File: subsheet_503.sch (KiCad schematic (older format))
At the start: 39 parts, among them Q500 LM78L82_TO92, U504 LF347N_mu, U505 MF4CN-100_PHY, U506 MF4CN-100_PHY, U507 LF347N_mu

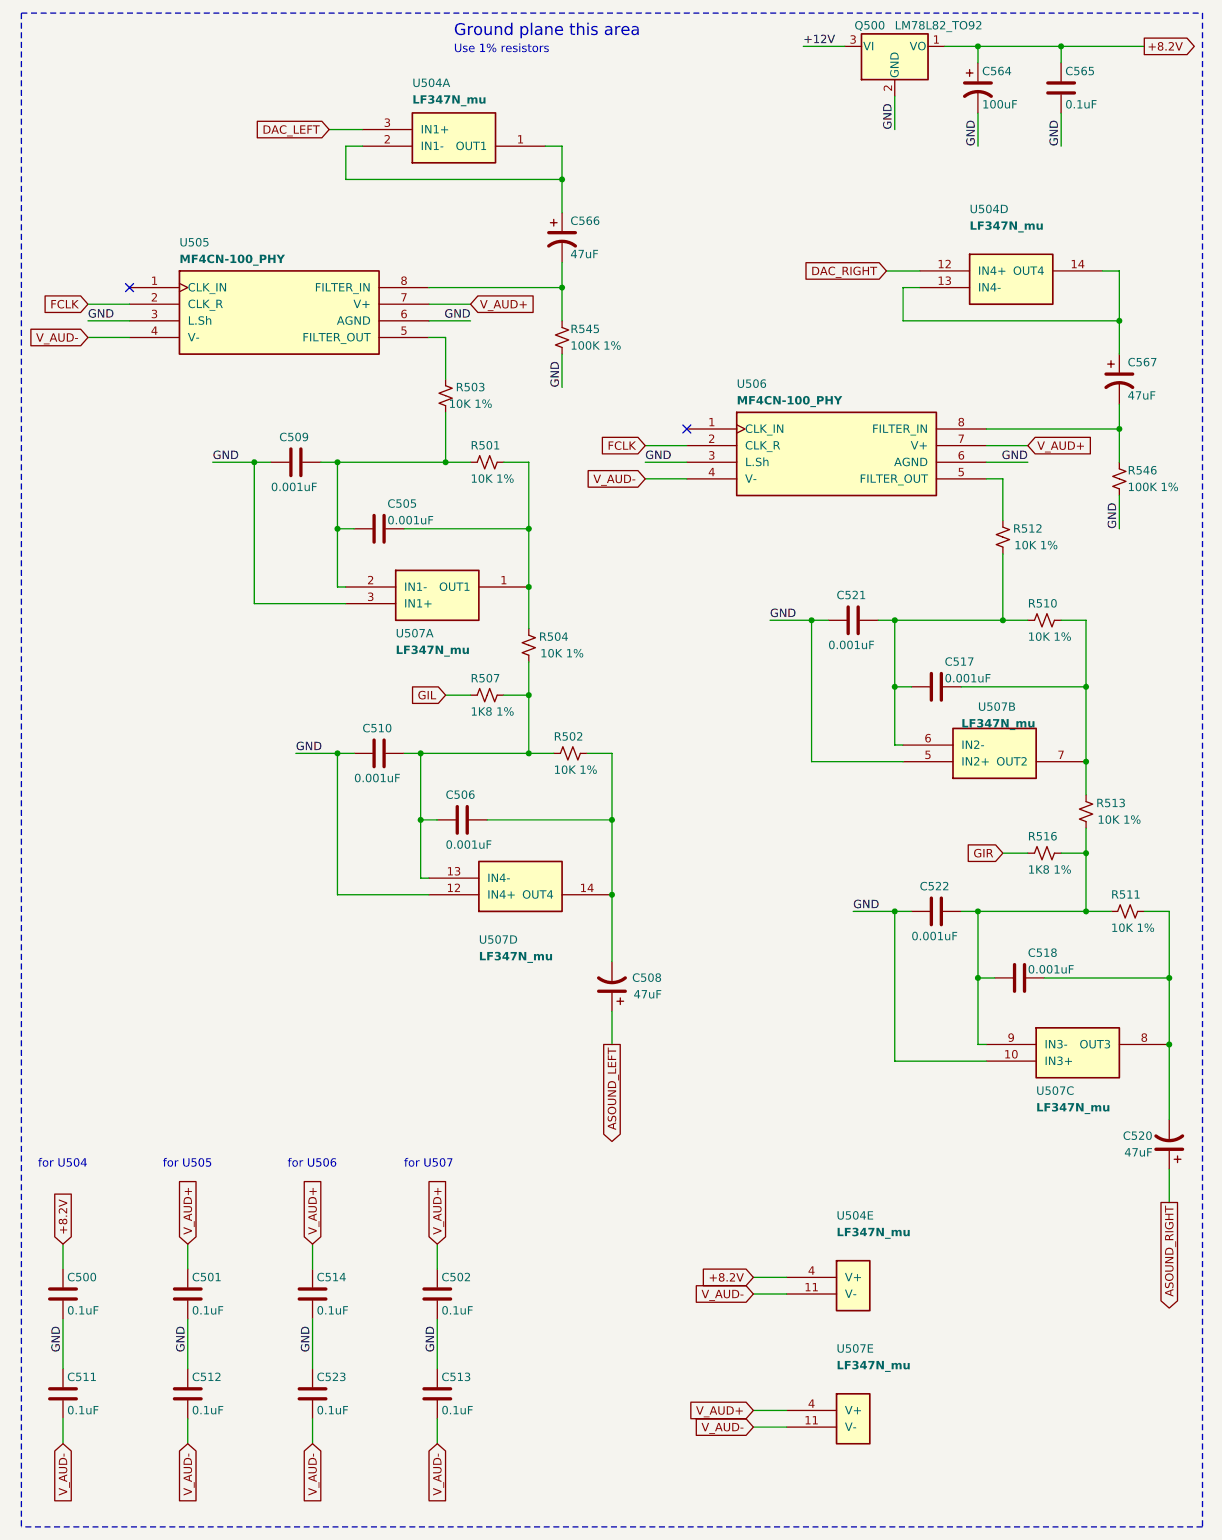
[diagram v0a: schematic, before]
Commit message: Resolves #12 : Use the reference 'CP?' for polarized capacitors
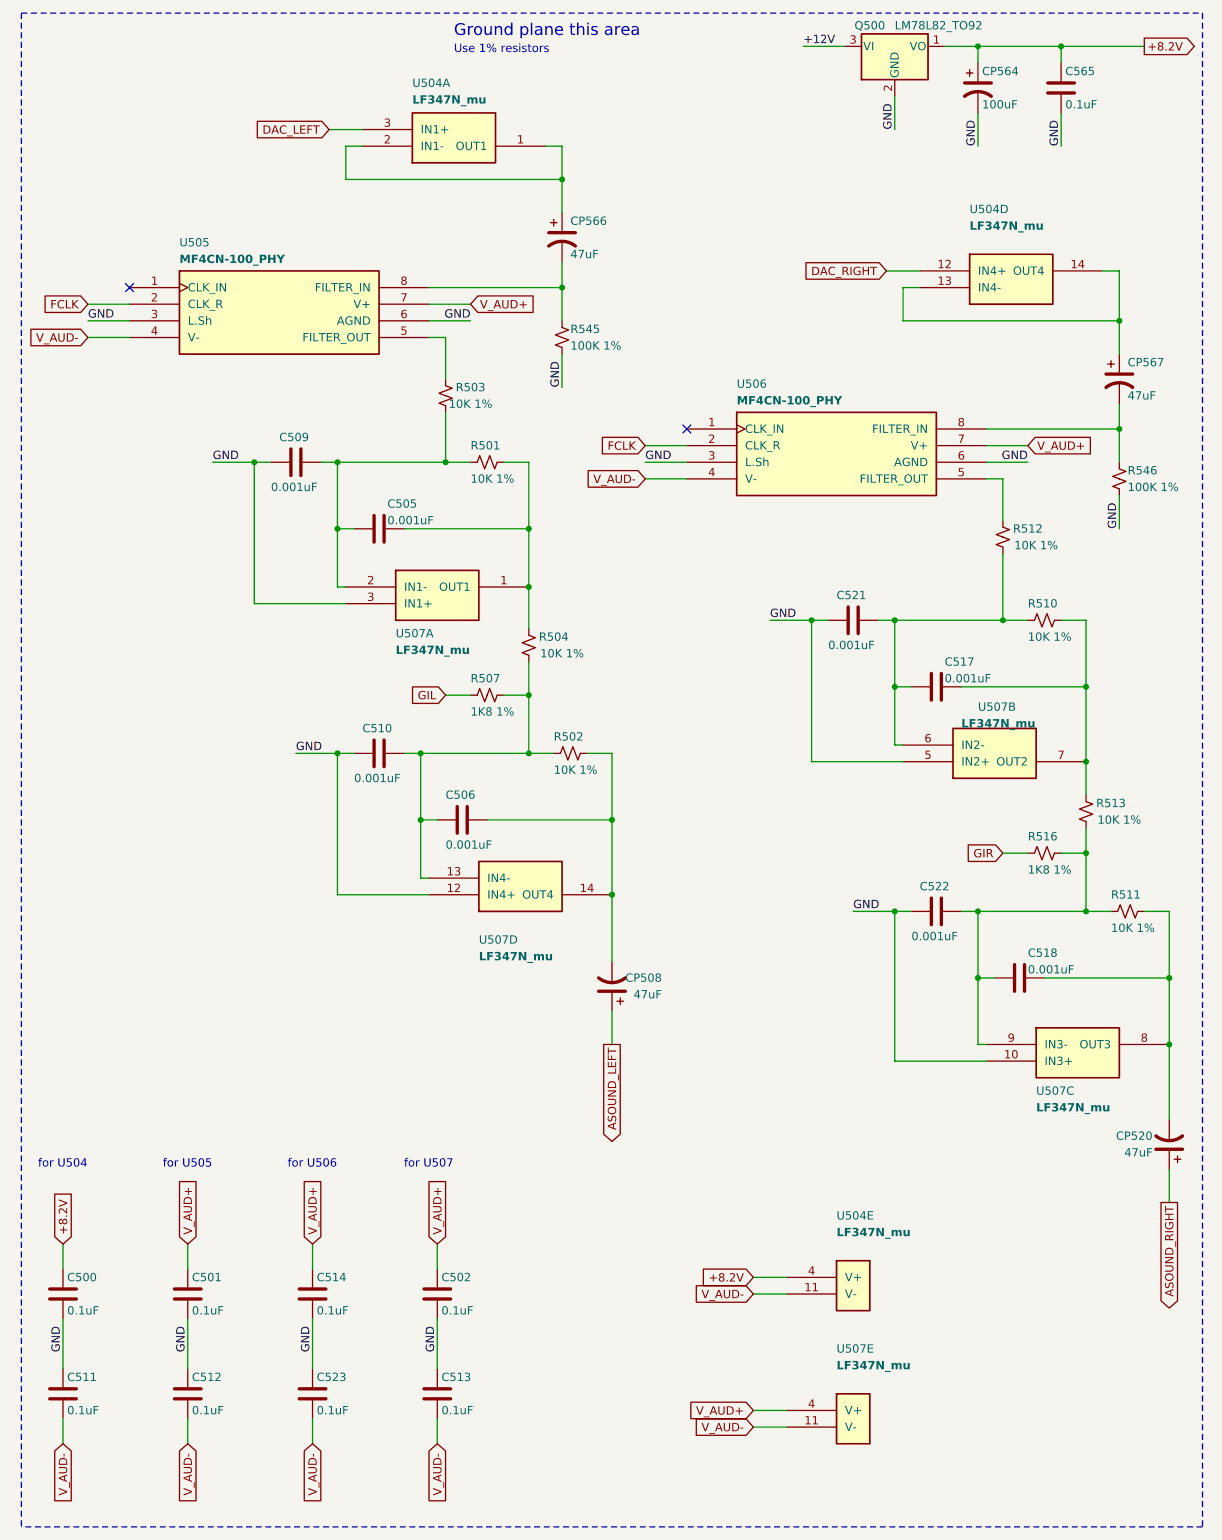
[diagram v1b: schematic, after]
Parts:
- renumbered C508 to CP508, C520 to CP520, C564 to CP564, C566 to CP566, C567 to CP567
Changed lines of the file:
@@
 AR Path="/60B8B7AD/60D196C8" Ref="C?"  Part="1"
 AR Path="/60C95DE8/60D196C8" Ref="C?"  Part="1"
-AR Path="/60CC3B10/60D196C8" Ref="C566"  Part="1"
-F 0 "C566" H 3900 2050 50  0000 L CNN
+AR Path="/60CC3B10/60D196C8" Ref="CP566"  Part="1"
+F 0 "CP566" H 3900 2050 50  0000 L CNN
 F 1 "47uF" H 3900 1850 50  0000 L CNN
 F 2 "commons_passives_THT:Passive_THT_capacitor_polarized_rad_D5.08mm_P2.54mm_H12.70mm" H 3850 1950 50  0001 C CNN
@@
 AR Path="/60B8B7AD/60DEF28D" Ref="C?"  Part="1"
 AR Path="/60C95DE8/60DEF28D" Ref="C?"  Part="1"
-AR Path="/60CC3B10/60DEF28D" Ref="C567"  Part="1"
-F 0 "C567" H 7250 2900 50  0000 L CNN
+AR Path="/60CC3B10/60DEF28D" Ref="CP567"  Part="1"
+F 0 "CP567" H 7250 2900 50  0000 L CNN
 F 1 "47uF" H 7250 2700 50  0000 L CNN
 F 2 "commons_passives_THT:Passive_THT_capacitor_polarized_rad_D5.08mm_P2.54mm_H12.70mm" H 7200 2800 50  0001 C CNN
@@
 AR Path="/60B8B7AD/60E9CB0E" Ref="C?"  Part="1"
 AR Path="/60C95DE8/60E9CB0E" Ref="C?"  Part="1"
-AR Path="/60CC3B10/60E9CB0E" Ref="C520"  Part="1"
-F 0 "C520" H 7600 7350 50  0000 L CNN
+AR Path="/60CC3B10/60E9CB0E" Ref="CP520"  Part="1"
+F 0 "CP520" H 7600 7350 50  0000 L CNN
 F 1 "47uF" H 7600 7450 50  0000 L CNN
 F 2 "commons_passives_THT:Passive_THT_capacitor_polarized_W6.35mm_L20.32mm" H 7500 7400 50  0001 C CNN
@@
 AR Path="/60B8B7AD/60E9CAAA" Ref="C?"  Part="1"
 AR Path="/60C95DE8/60E9CAAA" Ref="C?"  Part="1"
-AR Path="/60CC3B10/60E9CAAA" Ref="C508"  Part="1"
-F 0 "C508" H 3850 6400 50  0000 L CNN
+AR Path="/60CC3B10/60E9CAAA" Ref="CP508"  Part="1"
+F 0 "CP508" H 3850 6400 50  0000 L CNN
 F 1 "47uF" H 3850 6500 50  0000 L CNN
 F 2 "commons_passives_THT:Passive_THT_capacitor_polarized_W6.35mm_L20.32mm" H 4150 6450 50  0001 C CNN
@@
 AR Path="/60C95DE8/60E55789" Ref="C?"  Part="1"
 AR Path="/60CD36E9/60E55789" Ref="C?"  Part="1"
-AR Path="/60CC3B10/60E55789" Ref="C564"  Part="1"
-F 0 "C564" H 6375 1150 50  0000 L CNN
+AR Path="/60CC3B10/60E55789" Ref="CP564"  Part="1"
+F 0 "CP564" H 6375 1150 50  0000 L CNN
 F 1 "100uF" H 6375 950 50  0000 L CNN
 F 2 "commons_passives_THT:Passive_THT_capacitor_polarized_W6.35mm_L20.32mm" H 6350 1050 50  0001 C CNN

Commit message: Resolves #13 : assign 1206 hand-solder footprints to resistors
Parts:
- R501, R502, R503, R504, R507, R510, R511, R512, R513, R516, R545, R546: footprint commons_passives_THT:Passive_THT_resistor_W2.54mm_L12.70mm -> Resistor_SMD:R_1206_3216Metric_Pad1.30x1.75mm_HandSolder
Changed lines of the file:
@@
 F 0 "R545" H 3900 2600 50  0000 L CNN
 F 1 "100K 1%" H 3900 2500 50  0000 L CNN
-F 2 "commons_passives_THT:Passive_THT_resistor_W2.54mm_L12.70mm" H 3850 2550 50  0001 C CNN
+F 2 "Resistor_SMD:R_1206_3216Metric_Pad1.30x1.75mm_HandSolder" H 3850 2550 50  0001 C CNN
 F 3 "~" H 3850 2550 50  0001 C CNN
 	1    3850 2550
@@
 F 0 "R546" H 7250 3450 50  0000 L CNN
 F 1 "100K 1%" H 7250 3350 50  0000 L CNN
-F 2 "commons_passives_THT:Passive_THT_resistor_W2.54mm_L12.70mm" H 7200 3400 50  0001 C CNN
+F 2 "Resistor_SMD:R_1206_3216Metric_Pad1.30x1.75mm_HandSolder" H 7200 3400 50  0001 C CNN
 F 3 "~" H 7200 3400 50  0001 C CNN
 	1    7200 3400
@@
 F 0 "R513" H 6850 5350 50  0000 C CNN
 F 1 "10K 1%" H 6800 5450 50  0000 C CNN
-F 2 "commons_passives_THT:Passive_THT_resistor_W2.54mm_L12.70mm" H 7000 5400 50  0001 C CNN
+F 2 "Resistor_SMD:R_1206_3216Metric_Pad1.30x1.75mm_HandSolder" H 7000 5400 50  0001 C CNN
 F 3 "~" H 7000 5400 50  0001 C CNN
 	1    7000 5400
@@
 F 0 "R511" V 7150 5900 50  0000 L CNN
 F 1 "10K 1%" V 7350 5900 50  0000 L CNN
-F 2 "commons_passives_THT:Passive_THT_resistor_W2.54mm_L12.70mm" H 7250 6000 50  0001 C CNN
+F 2 "Resistor_SMD:R_1206_3216Metric_Pad1.30x1.75mm_HandSolder" H 7250 6000 50  0001 C CNN
 F 3 "~" H 7250 6000 50  0001 C CNN
 	1    7250 6000
@@
 F 0 "R512" H 6350 3700 50  0000 C CNN
 F 1 "10K 1%" H 6300 3800 50  0000 C CNN
-F 2 "commons_passives_THT:Passive_THT_resistor_W2.54mm_L12.70mm" H 6500 3750 50  0001 C CNN
+F 2 "Resistor_SMD:R_1206_3216Metric_Pad1.30x1.75mm_HandSolder" H 6500 3750 50  0001 C CNN
 F 3 "~" H 6500 3750 50  0001 C CNN
 	1    6500 3750
@@
 F 0 "R510" V 6650 4150 50  0000 L CNN
 F 1 "10K 1%" V 6850 4150 50  0000 L CNN
-F 2 "commons_passives_THT:Passive_THT_resistor_W2.54mm_L12.70mm" H 6750 4250 50  0001 C CNN
+F 2 "Resistor_SMD:R_1206_3216Metric_Pad1.30x1.75mm_HandSolder" H 6750 4250 50  0001 C CNN
 F 3 "~" H 6750 4250 50  0001 C CNN
 	1    6750 4250
@@
 F 0 "R516" V 6650 5550 50  0000 L CNN
 F 1 "1K8 1%" V 6850 5550 50  0000 L CNN
-F 2 "commons_passives_THT:Passive_THT_resistor_W2.54mm_L12.70mm" H 6750 5650 50  0001 C CNN
+F 2 "Resistor_SMD:R_1206_3216Metric_Pad1.30x1.75mm_HandSolder" H 6750 5650 50  0001 C CNN
 F 3 "~" H 6750 5650 50  0001 C CNN
 	1    6750 5650
@@
 F 0 "R504" H 3500 4350 50  0000 C CNN
 F 1 "10K 1%" H 3450 4450 50  0000 C CNN
-F 2 "commons_passives_THT:Passive_THT_resistor_W2.54mm_L12.70mm" H 3650 4400 50  0001 C CNN
+F 2 "Resistor_SMD:R_1206_3216Metric_Pad1.30x1.75mm_HandSolder" H 3650 4400 50  0001 C CNN
 F 3 "~" H 3650 4400 50  0001 C CNN
 	1    3650 4400
@@
 F 0 "R502" V 3800 4950 50  0000 L CNN
 F 1 "10K 1%" V 4000 4950 50  0000 L CNN
-F 2 "commons_passives_THT:Passive_THT_resistor_W2.54mm_L12.70mm" H 3900 5050 50  0001 C CNN
+F 2 "Resistor_SMD:R_1206_3216Metric_Pad1.30x1.75mm_HandSolder" H 3900 5050 50  0001 C CNN
 F 3 "~" H 3900 5050 50  0001 C CNN
 	1    3900 5050
@@
 F 0 "R503" H 3000 2850 50  0000 C CNN
 F 1 "10K 1%" H 3000 2950 50  0000 C CNN
-F 2 "commons_passives_THT:Passive_THT_resistor_W2.54mm_L12.70mm" H 3150 2900 50  0001 C CNN
+F 2 "Resistor_SMD:R_1206_3216Metric_Pad1.30x1.75mm_HandSolder" H 3150 2900 50  0001 C CNN
 F 3 "~" H 3150 2900 50  0001 C CNN
 	1    3150 2900
@@
 F 0 "R501" V 3300 3200 50  0000 L CNN
 F 1 "10K 1%" V 3500 3200 50  0000 L CNN
-F 2 "commons_passives_THT:Passive_THT_resistor_W2.54mm_L12.70mm" H 3400 3300 50  0001 C CNN
+F 2 "Resistor_SMD:R_1206_3216Metric_Pad1.30x1.75mm_HandSolder" H 3400 3300 50  0001 C CNN
 F 3 "~" H 3400 3300 50  0001 C CNN
 	1    3400 3300
@@
 F 0 "R507" V 3300 4600 50  0000 L CNN
 F 1 "1K8 1%" V 3500 4600 50  0000 L CNN
-F 2 "commons_passives_THT:Passive_THT_resistor_W2.54mm_L12.70mm" H 3400 4700 50  0001 C CNN
+F 2 "Resistor_SMD:R_1206_3216Metric_Pad1.30x1.75mm_HandSolder" H 3400 4700 50  0001 C CNN
 F 3 "~" H 3400 4700 50  0001 C CNN
 	1    3400 4700

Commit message: Resolves #8 : Assign 1206 hand-solder footprints to non polarized capacitors
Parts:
- C500, C501, C502, C511, C512, C513, C514, C523, C565: footprint commons_passives_THT:Passive_THT_capacitor_mlcc_W2.54mm_L7.62mm -> Capacitor_SMD:C_1206_3216Metric_Pad1.33x1.80mm_HandSolder
- C505, C506, C509, C510, C517, C518, C521, C522: footprint commons_passives_THT:Passive_THT_capacitor_W2.54mm_L10.16mm -> Capacitor_SMD:C_1206_3216Metric_Pad1.33x1.80mm_HandSolder
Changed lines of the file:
@@
 F 0 "C501" H 1625 8400 50  0000 L CNN
 F 1 "0.1uF" H 1625 8200 50  0000 L CNN
-F 2 "commons_passives_THT:Passive_THT_capacitor_mlcc_W2.54mm_L7.62mm" H 1638 8150 50  0001 C CNN
+F 2 "Capacitor_SMD:C_1206_3216Metric_Pad1.33x1.80mm_HandSolder" H 1638 8150 50  0001 C CNN
 F 3 "~" H 1600 8300 50  0001 C CNN
 	1    1600 8300
@@
 F 0 "C512" H 1625 9000 50  0000 L CNN
 F 1 "0.1uF" H 1625 8800 50  0000 L CNN
-F 2 "commons_passives_THT:Passive_THT_capacitor_mlcc_W2.54mm_L7.62mm" H 1638 8750 50  0001 C CNN
+F 2 "Capacitor_SMD:C_1206_3216Metric_Pad1.33x1.80mm_HandSolder" H 1638 8750 50  0001 C CNN
 F 3 "~" H 1600 8900 50  0001 C CNN
 	1    1600 8900
@@
 F 0 "C500" H 875 8400 50  0000 L CNN
 F 1 "0.1uF" H 875 8200 50  0000 L CNN
-F 2 "commons_passives_THT:Passive_THT_capacitor_mlcc_W2.54mm_L7.62mm" H 888 8150 50  0001 C CNN
+F 2 "Capacitor_SMD:C_1206_3216Metric_Pad1.33x1.80mm_HandSolder" H 888 8150 50  0001 C CNN
 F 3 "~" H 850 8300 50  0001 C CNN
 	1    850  8300
@@
 F 0 "C511" H 875 9000 50  0000 L CNN
 F 1 "0.1uF" H 875 8800 50  0000 L CNN
-F 2 "commons_passives_THT:Passive_THT_capacitor_mlcc_W2.54mm_L7.62mm" H 888 8750 50  0001 C CNN
+F 2 "Capacitor_SMD:C_1206_3216Metric_Pad1.33x1.80mm_HandSolder" H 888 8750 50  0001 C CNN
 F 3 "~" H 850 8900 50  0001 C CNN
 	1    850  8900
@@
 F 0 "C502" H 3125 8400 50  0000 L CNN
 F 1 "0.1uF" H 3125 8200 50  0000 L CNN
-F 2 "commons_passives_THT:Passive_THT_capacitor_mlcc_W2.54mm_L7.62mm" H 3138 8150 50  0001 C CNN
+F 2 "Capacitor_SMD:C_1206_3216Metric_Pad1.33x1.80mm_HandSolder" H 3138 8150 50  0001 C CNN
 F 3 "~" H 3100 8300 50  0001 C CNN
 	1    3100 8300
@@
 F 0 "C513" H 3125 9000 50  0000 L CNN
 F 1 "0.1uF" H 3125 8800 50  0000 L CNN
-F 2 "commons_passives_THT:Passive_THT_capacitor_mlcc_W2.54mm_L7.62mm" H 3138 8750 50  0001 C CNN
+F 2 "Capacitor_SMD:C_1206_3216Metric_Pad1.33x1.80mm_HandSolder" H 3138 8750 50  0001 C CNN
 F 3 "~" H 3100 8900 50  0001 C CNN
 	1    3100 8900
@@
 F 0 "C514" H 2375 8400 50  0000 L CNN
 F 1 "0.1uF" H 2375 8200 50  0000 L CNN
-F 2 "commons_passives_THT:Passive_THT_capacitor_mlcc_W2.54mm_L7.62mm" H 2388 8150 50  0001 C CNN
+F 2 "Capacitor_SMD:C_1206_3216Metric_Pad1.33x1.80mm_HandSolder" H 2388 8150 50  0001 C CNN
 F 3 "~" H 2350 8300 50  0001 C CNN
 	1    2350 8300
@@
 F 0 "C523" H 2375 9000 50  0000 L CNN
 F 1 "0.1uF" H 2375 8800 50  0000 L CNN
-F 2 "commons_passives_THT:Passive_THT_capacitor_mlcc_W2.54mm_L7.62mm" H 2388 8750 50  0001 C CNN
+F 2 "Capacitor_SMD:C_1206_3216Metric_Pad1.33x1.80mm_HandSolder" H 2388 8750 50  0001 C CNN
 F 3 "~" H 2350 8900 50  0001 C CNN
 	1    2350 8900
@@
 F 0 "C518" V 6450 6450 50  0000 L CNN
 F 1 "0.001uF" V 6550 6450 50  0000 L CNN
-F 2 "commons_passives_THT:Passive_THT_capacitor_W2.54mm_L10.16mm" H 6638 6250 50  0001 C CNN
+F 2 "Capacitor_SMD:C_1206_3216Metric_Pad1.33x1.80mm_HandSolder" H 6638 6250 50  0001 C CNN
 F 3 "~" H 6600 6400 50  0001 C CNN
 	1    6600 6400
@@
 F 0 "C522" V 5950 5900 50  0000 L CNN
 F 1 "0.001uF" V 6250 5850 50  0000 L CNN
-F 2 "commons_passives_THT:Passive_THT_capacitor_W2.54mm_L10.16mm" H 6138 5850 50  0001 C CNN
+F 2 "Capacitor_SMD:C_1206_3216Metric_Pad1.33x1.80mm_HandSolder" H 6138 5850 50  0001 C CNN
 F 3 "~" H 6100 6000 50  0001 C CNN
 	1    6100 6000
@@
 F 0 "C517" V 5950 4700 50  0000 L CNN
 F 1 "0.001uF" V 6050 4700 50  0000 L CNN
-F 2 "commons_passives_THT:Passive_THT_capacitor_W2.54mm_L10.16mm" H 6138 4500 50  0001 C CNN
+F 2 "Capacitor_SMD:C_1206_3216Metric_Pad1.33x1.80mm_HandSolder" H 6138 4500 50  0001 C CNN
 F 3 "~" H 6100 4650 50  0001 C CNN
 	1    6100 4650
@@
 F 0 "C521" V 5450 4150 50  0000 L CNN
 F 1 "0.001uF" V 5750 4100 50  0000 L CNN
-F 2 "commons_passives_THT:Passive_THT_capacitor_W2.54mm_L10.16mm" H 5638 4100 50  0001 C CNN
+F 2 "Capacitor_SMD:C_1206_3216Metric_Pad1.33x1.80mm_HandSolder" H 5638 4100 50  0001 C CNN
 F 3 "~" H 5600 4250 50  0001 C CNN
 	1    5600 4250
@@
 F 0 "C506" V 3100 5350 50  0000 L CNN
 F 1 "0.001uF" V 3400 5350 50  0000 L CNN
-F 2 "commons_passives_THT:Passive_THT_capacitor_W2.54mm_L10.16mm" H 3288 5300 50  0001 C CNN
+F 2 "Capacitor_SMD:C_1206_3216Metric_Pad1.33x1.80mm_HandSolder" H 3288 5300 50  0001 C CNN
 F 3 "~" H 3250 5450 50  0001 C CNN
 	1    3250 5450
@@
 F 0 "C510" V 2600 4950 50  0000 L CNN
 F 1 "0.001uF" V 2900 4900 50  0000 L CNN
-F 2 "commons_passives_THT:Passive_THT_capacitor_W2.54mm_L10.16mm" H 2788 4900 50  0001 C CNN
+F 2 "Capacitor_SMD:C_1206_3216Metric_Pad1.33x1.80mm_HandSolder" H 2788 4900 50  0001 C CNN
 F 3 "~" H 2750 5050 50  0001 C CNN
 	1    2750 5050
@@
 F 0 "C505" V 2600 3750 50  0000 L CNN
 F 1 "0.001uF" V 2700 3750 50  0000 L CNN
-F 2 "commons_passives_THT:Passive_THT_capacitor_W2.54mm_L10.16mm" H 2788 3550 50  0001 C CNN
+F 2 "Capacitor_SMD:C_1206_3216Metric_Pad1.33x1.80mm_HandSolder" H 2788 3550 50  0001 C CNN
 F 3 "~" H 2750 3700 50  0001 C CNN
 	1    2750 3700
@@
 F 0 "C509" V 2100 3200 50  0000 L CNN
 F 1 "0.001uF" V 2400 3150 50  0000 L CNN
-F 2 "commons_passives_THT:Passive_THT_capacitor_W2.54mm_L10.16mm" H 2288 3150 50  0001 C CNN
+F 2 "Capacitor_SMD:C_1206_3216Metric_Pad1.33x1.80mm_HandSolder" H 2288 3150 50  0001 C CNN
 F 3 "~" H 2250 3300 50  0001 C CNN
 	1    2250 3300
@@
 F 0 "C565" H 6875 1150 50  0000 L CNN
 F 1 "0.1uF" H 6875 950 50  0000 L CNN
-F 2 "commons_passives_THT:Passive_THT_capacitor_mlcc_W2.54mm_L7.62mm" H 6888 900 50  0001 C CNN
+F 2 "Capacitor_SMD:C_1206_3216Metric_Pad1.33x1.80mm_HandSolder" H 6888 900 50  0001 C CNN
 F 3 "~" H 6850 1050 50  0001 C CNN
 	1    6850 1050

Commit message: Resolves #9 : Assign radial THT footprints to polarized capacitors
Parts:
- CP508, CP520: footprint commons_passives_THT:Passive_THT_capacitor_polarized_W6.35mm_L20.32mm -> Capacitor_THT:C_Radial_D6.3mm_H11.0mm_P2.50mm
- CP564: footprint commons_passives_THT:Passive_THT_capacitor_polarized_W6.35mm_L20.32mm -> Capacitor_THT:C_Radial_D8.0mm_H11.5mm_P3.50mm
- CP566, CP567: footprint commons_passives_THT:Passive_THT_capacitor_polarized_rad_D5.08mm_P2.54mm_H12.70mm -> Capacitor_THT:C_Radial_D6.3mm_H11.0mm_P2.50mm
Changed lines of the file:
@@
 F 0 "CP566" H 3900 2050 50  0000 L CNN
 F 1 "47uF" H 3900 1850 50  0000 L CNN
-F 2 "commons_passives_THT:Passive_THT_capacitor_polarized_rad_D5.08mm_P2.54mm_H12.70mm" H 3850 1950 50  0001 C CNN
+F 2 "Capacitor_THT:C_Radial_D6.3mm_H11.0mm_P2.50mm" H 3850 1950 50  0001 C CNN
 F 3 "~" H 3850 1950 50  0001 C CNN
 	1    3850 1950
@@
 F 0 "CP567" H 7250 2900 50  0000 L CNN
 F 1 "47uF" H 7250 2700 50  0000 L CNN
-F 2 "commons_passives_THT:Passive_THT_capacitor_polarized_rad_D5.08mm_P2.54mm_H12.70mm" H 7200 2800 50  0001 C CNN
+F 2 "Capacitor_THT:C_Radial_D6.3mm_H11.0mm_P2.50mm" H 7200 2800 50  0001 C CNN
 F 3 "~" H 7200 2800 50  0001 C CNN
 	1    7200 2800
@@
 F 0 "CP520" H 7600 7350 50  0000 L CNN
 F 1 "47uF" H 7600 7450 50  0000 L CNN
-F 2 "commons_passives_THT:Passive_THT_capacitor_polarized_W6.35mm_L20.32mm" H 7500 7400 50  0001 C CNN
+F 2 "Capacitor_THT:C_Radial_D6.3mm_H11.0mm_P2.50mm" H 7500 7400 50  0001 C CNN
 F 3 "~" H 7500 7400 50  0001 C CNN
 	1    7500 7400
@@
 F 0 "CP508" H 3850 6400 50  0000 L CNN
 F 1 "47uF" H 3850 6500 50  0000 L CNN
-F 2 "commons_passives_THT:Passive_THT_capacitor_polarized_W6.35mm_L20.32mm" H 4150 6450 50  0001 C CNN
+F 2 "Capacitor_THT:C_Radial_D6.3mm_H11.0mm_P2.50mm" H 4150 6450 50  0001 C CNN
 F 3 "~" H 4150 6450 50  0001 C CNN
 	1    4150 6450
@@
 F 0 "CP564" H 6375 1150 50  0000 L CNN
 F 1 "100uF" H 6375 950 50  0000 L CNN
-F 2 "commons_passives_THT:Passive_THT_capacitor_polarized_W6.35mm_L20.32mm" H 6350 1050 50  0001 C CNN
+F 2 "Capacitor_THT:C_Radial_D8.0mm_H11.5mm_P3.50mm" H 6350 1050 50  0001 C CNN
 F 3 "~" H 6350 1050 50  0001 C CNN
 	1    6350 1050

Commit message: Resolves #17 : assign smd footprints to transistors
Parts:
- Q500: footprint Package_TO_SOT_THT:TO-92_Inline_Wide -> Package_TO_SOT_SMD:SOT-89-3_Handsoldering
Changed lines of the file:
@@
 F 0 "Q500" H 5700 925 50  0000 C CNN
 F 1 "LM78L82_TO92" H 5850 925 50  0000 L CNN
-F 2 "Package_TO_SOT_THT:TO-92_Inline_Wide" H 5850 1025 50  0001 C CIN
+F 2 "Package_TO_SOT_SMD:SOT-89-3_Handsoldering" H 5850 1025 50  0001 C CIN
 F 3 "https://www.onsemi.com/pub/Collateral/MC78L06A-D.pdf" H 5850 750 50  0001 C CNN
 	1    5850 800
